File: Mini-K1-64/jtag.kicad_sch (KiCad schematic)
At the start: 4 parts

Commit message: Format PCB
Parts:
- renumbered R5 to R6, R4 to R9
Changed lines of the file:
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@@
 		(dnp no)
 		(fields_autoplaced yes)
-		(property "Reference" "R5"
+		(property "Reference" "R6"
 			(at 153.67 113.0299 0)
 			(effects
@@
 			(project "Mini-K1-64"
 				(path "/1a7e0d91-a6c0-4b42-a7c6-42574ab26c7c/d40cf31c-d44b-4043-95be-87a4586e4753"
-					(reference "R5")
+					(reference "R6")
 					(unit 1)
 				)
@@
 		(dnp no)
 		(fields_autoplaced yes)
-		(property "Reference" "R4"
+		(property "Reference" "R9"
 			(at 157.48 92.7099 0)
 			(effects
@@
 			(project "Mini-K1-64"
 				(path "/1a7e0d91-a6c0-4b42-a7c6-42574ab26c7c/d40cf31c-d44b-4043-95be-87a4586e4753"
-					(reference "R4")
-					(unit 1)
-				)
+					(reference "R9")
+					(unit 1)
+				)

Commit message: Rev0
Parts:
- renumbered J1 to J2
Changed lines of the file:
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@@
 		(dnp no)
 		(fields_autoplaced yes)
-		(property "Reference" "J1"
+		(property "Reference" "J2"
 			(at 132.08 90.17 0)
 			(effects
@@
 			(project "Mini-K1-64"
 				(path "/1a7e0d91-a6c0-4b42-a7c6-42574ab26c7c/d40cf31c-d44b-4043-95be-87a4586e4753"
-					(reference "J1")
+					(reference "J2")
 					(unit 1)
 				)

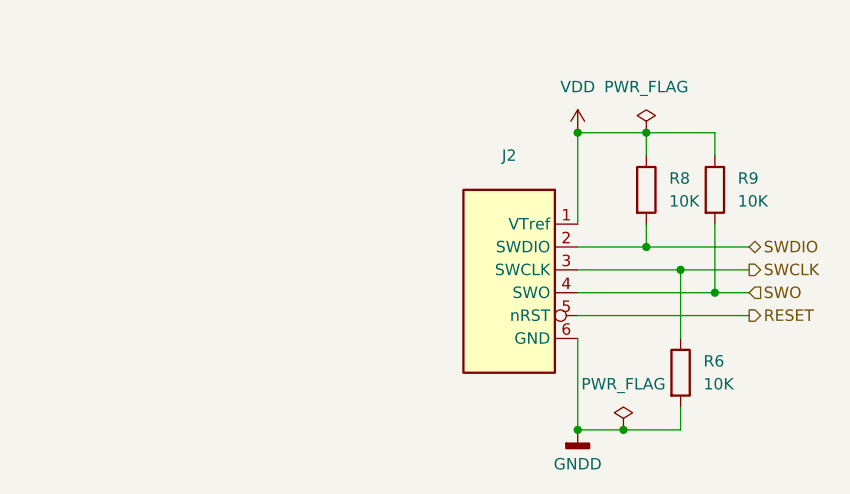
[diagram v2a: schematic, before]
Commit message: Update Debug Connector
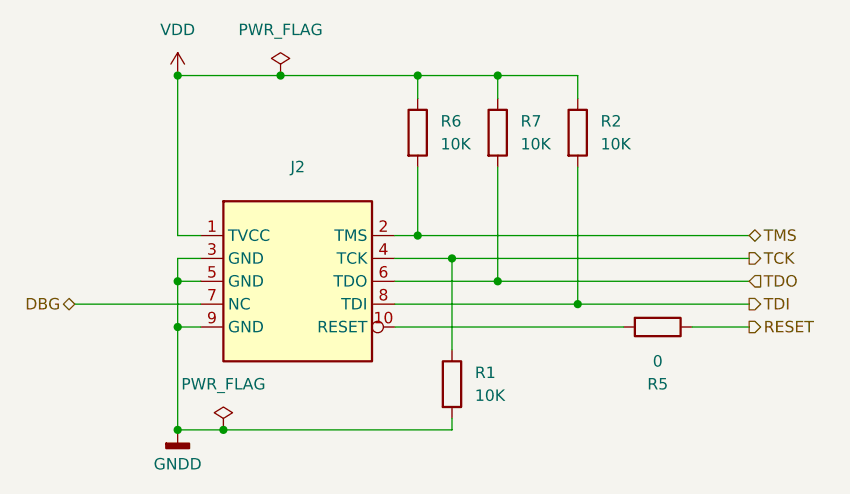
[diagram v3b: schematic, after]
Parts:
- removed J2: ~, Connector_PinHeader_2.54mm:PinHeader_1x06_P2.54mm_Vertical, symbol MCU_NXP_S32K1:SWD_6P
- added J2: ~, Connector_PinHeader_1.27mm:PinHeader_2x05_P1.27mm_Vertical, symbol MCU_NXP_S32K1:ARM_10P
- added R2: 10K, Resistor_SMD:R_0805_2012Metric, symbol Device:R
- added R5: 0, Resistor_SMD:R_0805_2012Metric, symbol Device:R
- renumbered R6 to R1, R8 to R6, R9 to R7
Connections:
- net GNDD: now also J2.3 (GND), J2.5 (GND), J2.9 (GND)
- net RESET: now also R5.1
- net VDD: now also J2.1 (TVCC), R2.1
- net SWCLK renamed TCK
- net TCK: now also J2.4 (TCK)
- net SWDIO renamed TMS
- net TMS: now also J2.2 (TMS)
- net SWO renamed TDO
- net TDO: now also J2.6 (TDO)
- new net: J2.10 (RESET), R5.2
- new net DBG: J2.7 (NC)
- new net TDI: J2.8 (TDI), R2.2
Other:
- moved on the sheet: R1, R6, R7
